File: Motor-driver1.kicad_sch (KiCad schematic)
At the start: 56 parts, among them J3 PINHD_1x3_Male, J4 PINHD_1x3_Male, J5 PINHD_1x3_Male, J7 PINHD_1x3_Male, J8 PINHD_1x4_Male, J9 PINHD_1x4_Male, U2 DRV8825PWP, U3 DRV8825PWP

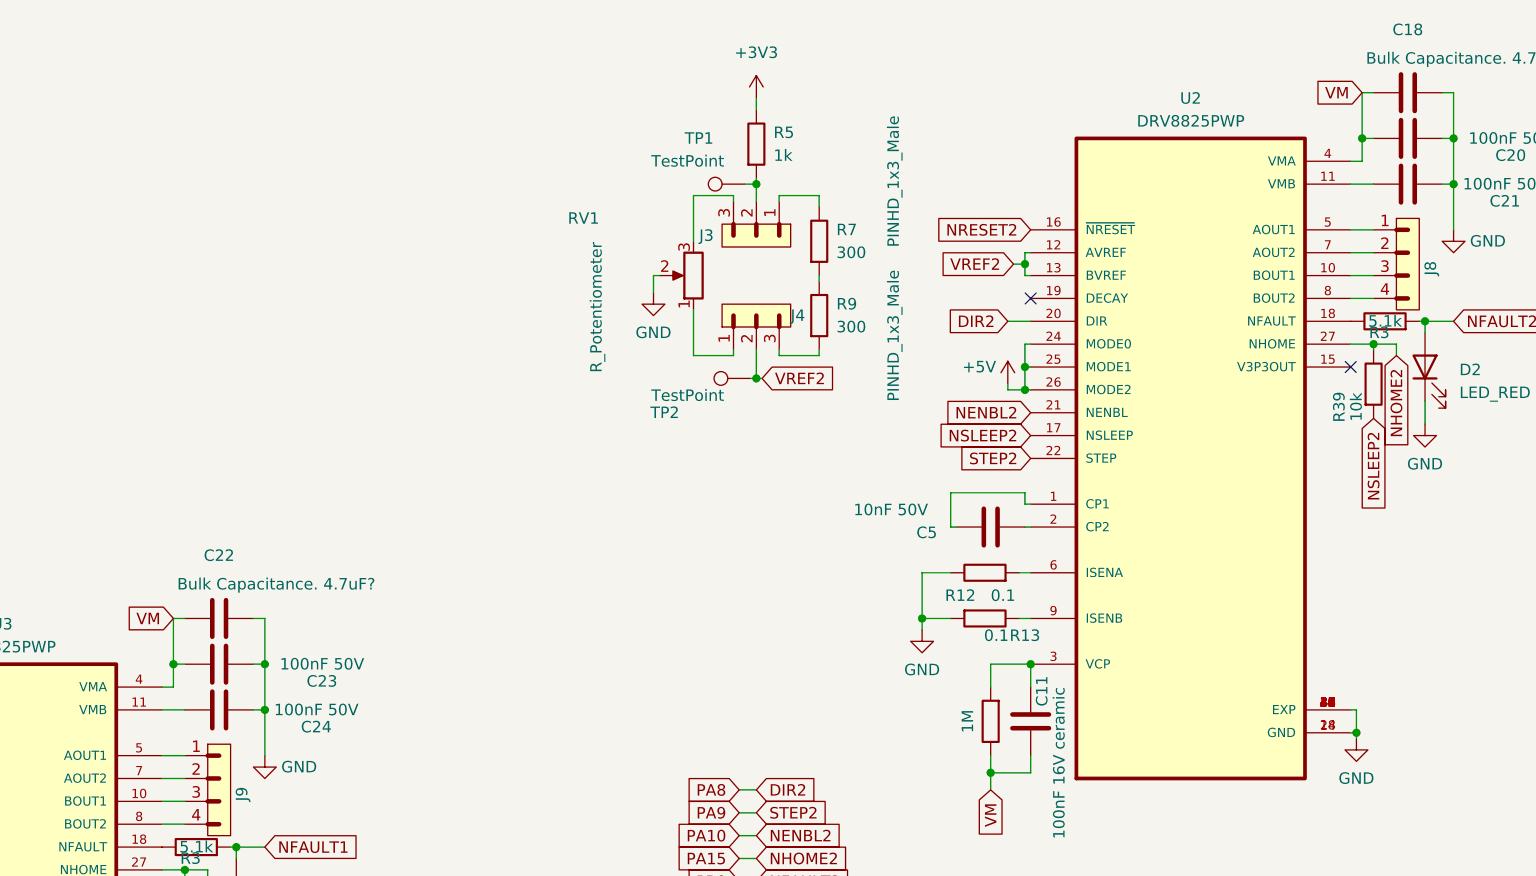
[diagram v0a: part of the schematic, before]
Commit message: fixed few errors, added test points
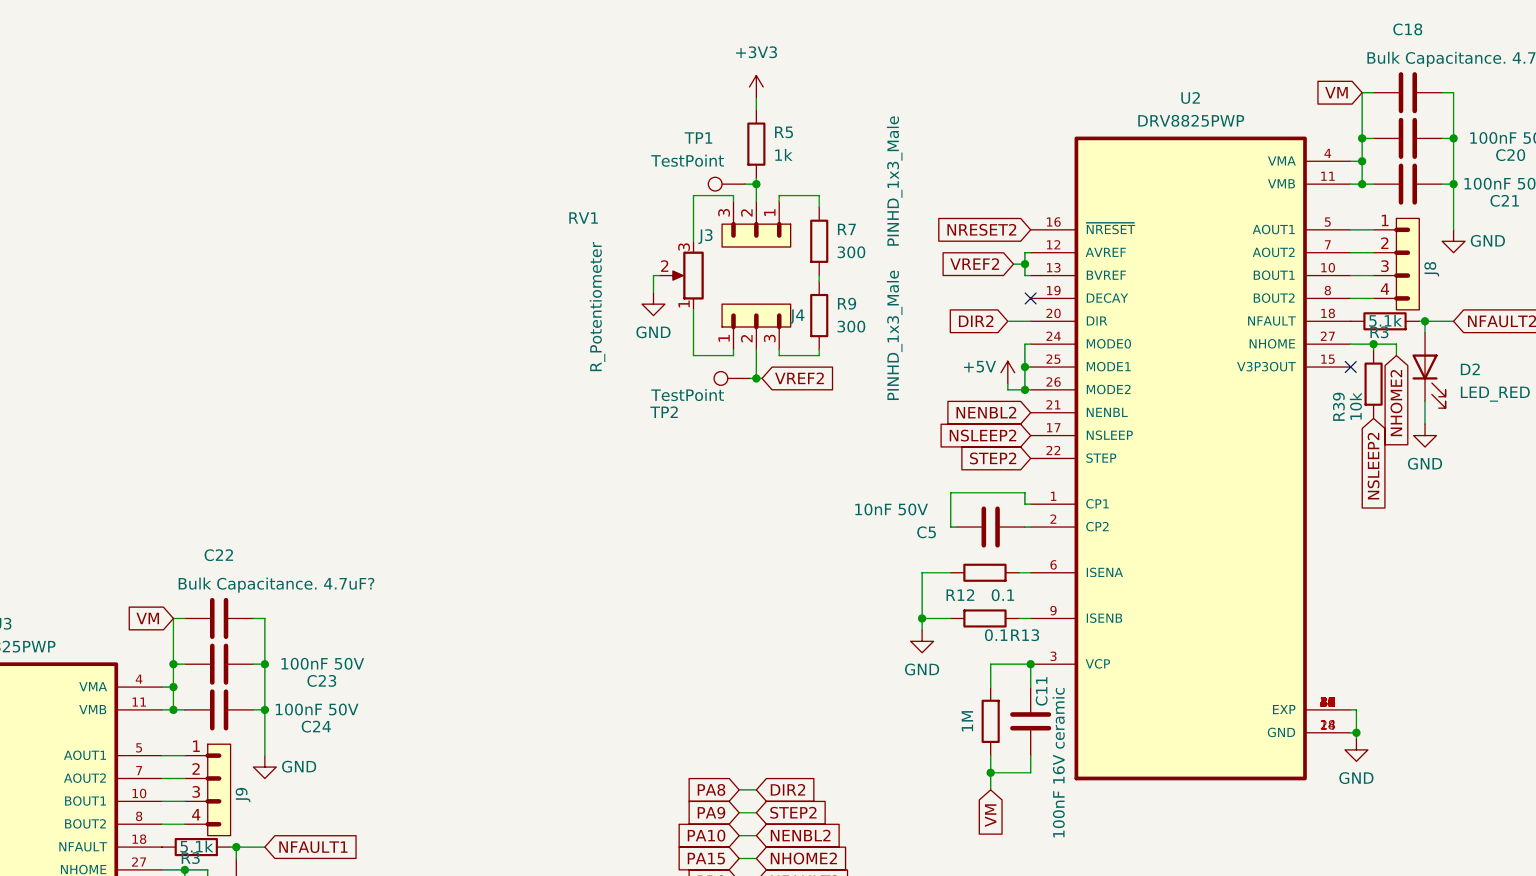
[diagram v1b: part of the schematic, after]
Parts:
- C11, C16: footprint (none) -> Capacitor_SMD:C_01005_0402Metric
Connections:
- net VM: now also C21.1, C24.1, U2.11 (VMB), U3.11 (VMB)
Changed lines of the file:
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@@
   (junction (at 219.075 97.79) (diameter 0) (color 0 0 0 0)
   )
+  (junction (at 255.905 41.91) (diameter 0) (color 0 0 0 0)
+  )
   (junction (at 133.985 97.79) (diameter 0) (color 0 0 0 0)
   )
@@
   (junction (at 262.89 59.69) (diameter 0) (color 0 0 0 0)
   )
+  (junction (at 255.905 44.45) (diameter 0) (color 0 0 0 0)
+  )
   (junction (at 218.44 67.31) (diameter 0) (color 0 0 0 0)
   )
@@
   (junction (at 74.93 151.13) (diameter 0) (color 0 0 0 0)
   )
+  (junction (at 123.825 100.33) (diameter 0) (color 0 0 0 0)
+  )
   (junction (at 188.595 44.45) (diameter 0) (color 0 0 0 0)
   )
@@
   )
   (junction (at 125.095 120.65) (diameter 0) (color 0 0 0 0)
+  )
+  (junction (at 123.825 102.87) (diameter 0) (color 0 0 0 0)
   )
   (junction (at 82.55 168.275) (diameter 0) (color 0 0 0 0)
@@
     (stroke (width 0) (type default))
   )
-  (wire (pts (xy 254.635 44.45) (xy 257.175 44.45))
+  (wire (pts (xy 254.635 44.45) (xy 255.905 44.45))
     (stroke (width 0) (type default))
   )
@@
     (stroke (width 0) (type default))
   )
+  (wire (pts (xy 255.905 41.91) (xy 255.905 44.45))
+    (stroke (width 0) (type default))
+  )
   (wire (pts (xy 191.135 140.335) (xy 191.135 139.7))
     (stroke (width 0) (type default))
@@
     (stroke (width 0) (type default))
   )
+  (wire (pts (xy 255.905 44.45) (xy 257.175 44.45))
+    (stroke (width 0) (type default))
+  )
   (wire (pts (xy 43.18 82.55) (xy 43.18 81.915))
     (stroke (width 0) (type default))
@@
     (stroke (width 0) (type default))
   )
+  (wire (pts (xy 123.825 100.33) (xy 123.825 102.87))
+    (stroke (width 0) (type default))
+  )
   (wire (pts (xy 187.96 66.04) (xy 188.595 66.04))
     (stroke (width 0) (type default))
@@
     (stroke (width 0) (type default))
   )
+  (wire (pts (xy 123.825 102.87) (xy 125.095 102.87))
+    (stroke (width 0) (type default))
+  )
   (wire (pts (xy 264.795 44.45) (xy 266.065 44.45))
     (stroke (width 0) (type default))
@@
     (stroke (width 0) (type default))
   )
-  (wire (pts (xy 122.555 102.87) (xy 125.095 102.87))
+  (wire (pts (xy 122.555 102.87) (xy 123.825 102.87))
     (stroke (width 0) (type default))
   )
@@
       (effects (font (size 1.27 1.27)) (justify left))
     )
-    (property "Footprint" "" (at 86.0298 158.75 0)
+    (property "Footprint" "Capacitor_SMD:C_01005_0402Metric" (at 86.0298 158.75 0)
       (effects (font (size 1.27 1.27)) hide)
     )
@@
       (effects (font (size 1.27 1.27)) (justify left))
     )
-    (property "Footprint" "" (at 218.1098 100.33 0)
-      (effects (font (size 1.27 1.27)) hide)
-    )
+    (property "Footprint" "Capacitor_SMD:C_01005_0402Metric" (at 218.1098 100.33 0)
+      (effects (font (size 1.27 1.27)) hide)
+    )
